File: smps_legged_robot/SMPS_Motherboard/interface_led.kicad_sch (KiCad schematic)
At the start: 4 parts

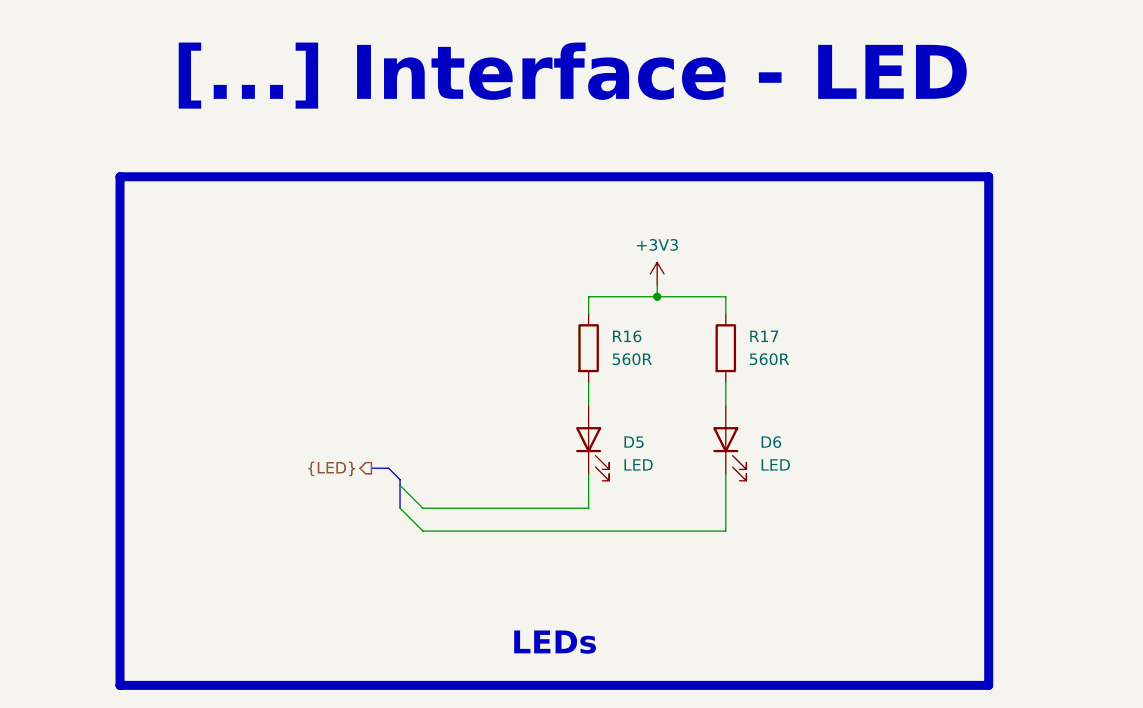
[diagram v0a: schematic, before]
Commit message: Buck module finished pending review
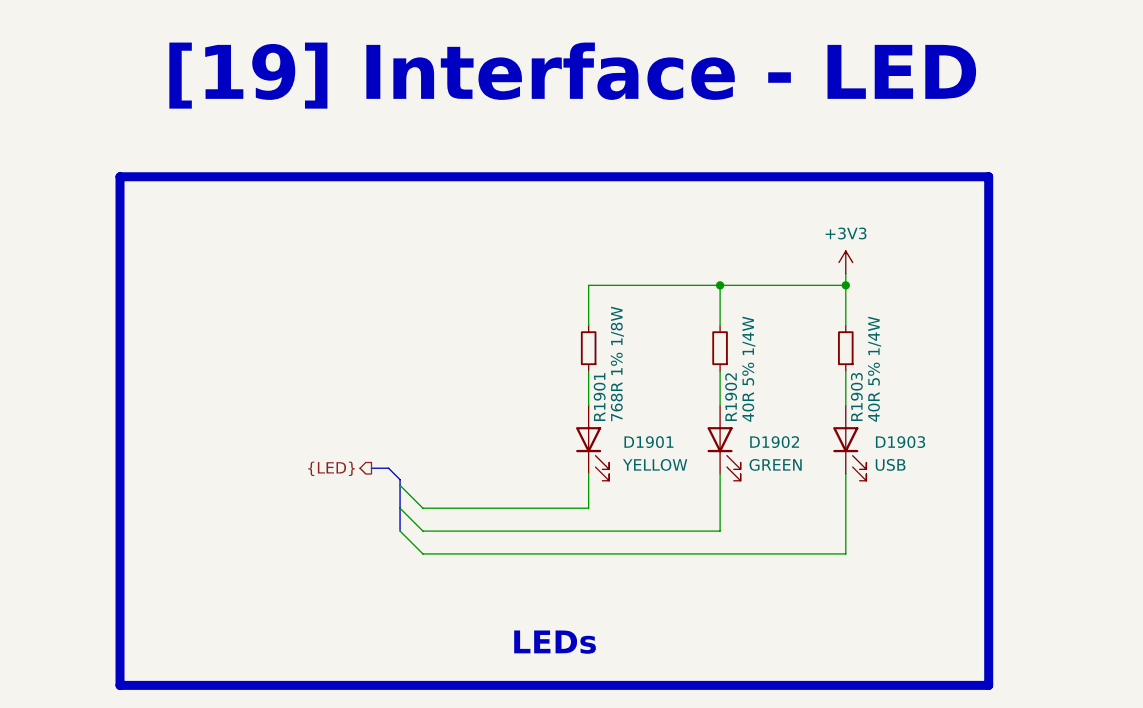
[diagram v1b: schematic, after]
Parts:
- removed D5, D6: LED, LED_SMD:LED_0603_1608Metric, symbol Device:LED
- removed R16, R17: 560R, 0_resistor_smd:R_0402_1005_DensityHigh, symbol Device:R
- added D1901: YELLOW, LED_SMD:LED_0603_1608Metric, symbol Device:LED
- added D1902: GREEN, LED_SMD:LED_0603_1608Metric, symbol Device:LED
- added D1903: USB, LED_SMD:LED_0603_1608Metric, symbol Device:LED
- added R1901: 768R 1% 1/8W, Resistor_SMD:R_0603_1608Metric, symbol Device:R_Small
- added R1902, R1903: 40R 5% 1/4W, Resistor_SMD:R_0603_1608Metric, symbol Device:R_Small
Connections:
- net +3V3: now also R1901.2, R1902.2, R1903.2
- new net: D1903.2 (A), R1903.1
- new net: D1901.2 (A), R1901.1
- new net: D1902.2 (A), R1902.1

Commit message: Rev 1.0 of smps finished -> waiting for verification
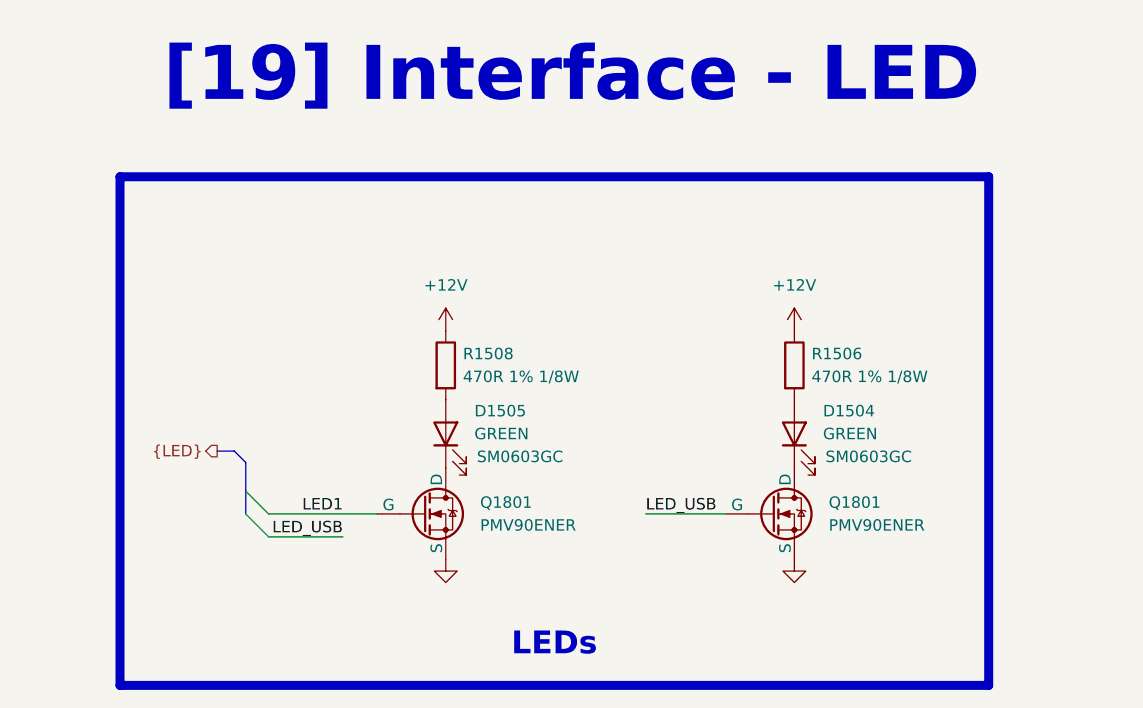
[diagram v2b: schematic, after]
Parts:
- removed D1901: YELLOW, LED_SMD:LED_0603_1608Metric, symbol Device:LED
- removed D1902: GREEN, LED_SMD:LED_0603_1608Metric, symbol Device:LED
- removed D1903: USB, LED_SMD:LED_0603_1608Metric, symbol Device:LED
- removed R1901: 768R 1% 1/8W, Resistor_SMD:R_0603_1608Metric, symbol Device:R_Small
- removed R1902, R1903: 40R 5% 1/4W, Resistor_SMD:R_0603_1608Metric, symbol Device:R_Small
- added D1504, D1505: GREEN, LED_SMD:LED_0603_1608Metric, symbol Device:LED
- added Q1801 (x2): PMV90ENER, 0_package_SOT_TO_SMD:SOT-23-3, symbol Simulation_SPICE:NMOS
- added R1506, R1508: 470R 1% 1/8W, 0_resistor_smd:R_0402_1005_DensityHigh, symbol Device:R
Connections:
- new net: D1505.2 (A), R1508.2
- new net: D1504.1 (K), Q1801.3 (D)
- new net: D1504.2 (A), R1506.2
- new net: D1505.1 (K), Q1801.3 (D)
- new net +12V: R1506.1, R1508.1
- new net GND: Q1801.2 (S), Q1801.2 (S)
- new net LED1: Q1801.1 (G)
- new net LED_USB: Q1801.1 (G)

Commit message: Geode test board ready to order
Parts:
- removed D1504, D1505: GREEN, LED_SMD:LED_0603_1608Metric, symbol Device:LED
- removed Q1801 (x2): PMV90ENER, 0_package_SOT_TO_SMD:SOT-23-3, symbol Simulation_SPICE:NMOS
- removed R1506, R1508: 470R 1% 1/8W, 0_resistor_smd:R_0402_1005_DensityHigh, symbol Device:R
